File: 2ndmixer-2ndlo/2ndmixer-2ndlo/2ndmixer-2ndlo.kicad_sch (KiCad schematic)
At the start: 55 parts, among them J201 Coax Solder Point, J202 Conn_01x02, J203 Coax Solder Point, Q201 2N5179, Q202 2N5109, T201 Bifilar_Transformer, U201 MAV-11BSM+, U202 TUF-1H+, Y201 100MHz

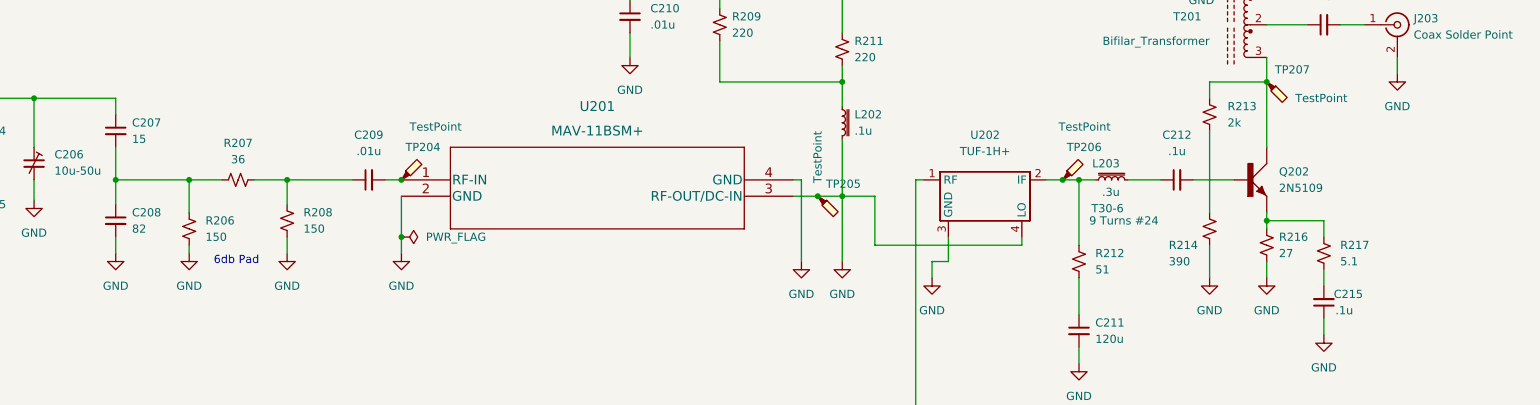
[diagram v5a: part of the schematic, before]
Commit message: added some test points
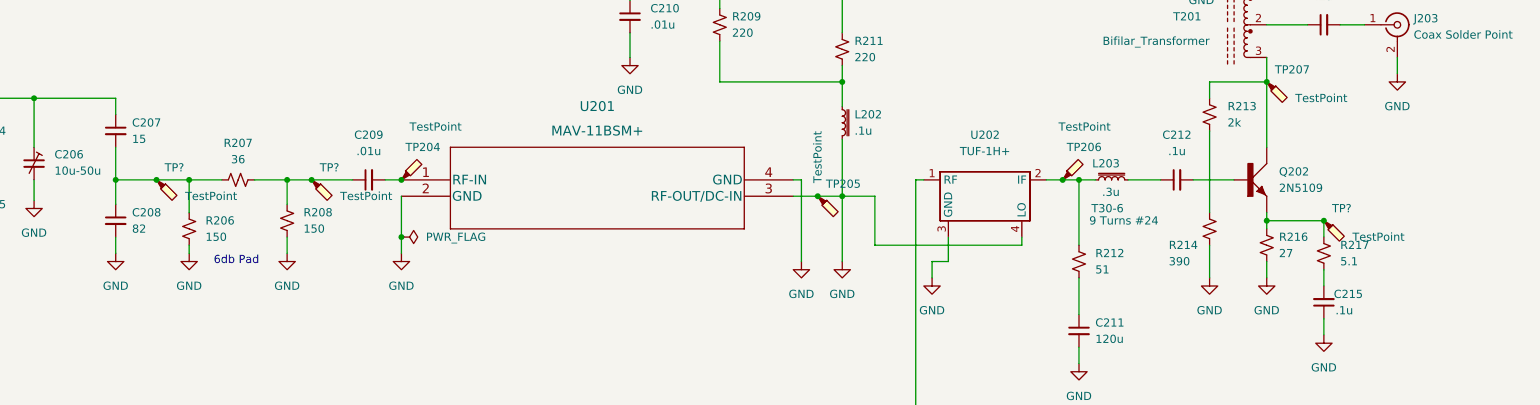
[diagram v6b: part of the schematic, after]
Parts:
- added TP? (x3): TestPoint, TestPoint:TestPoint_Pad_1.0x1.0mm, symbol Connector:TestPoint_Probe
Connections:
- net at C209.1, R207.2, R208.1: now also TP?.1
- net at Q202.E, R216.1, R217.1: now also TP?.1
- net at C207.2, C208.1, R206.1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: now also TP?.1
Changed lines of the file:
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@@
   (junction (at 49.53 69.85) (diameter 0) (color 0 0 0 0)
   )
+  (junction (at 123.19 120.65) (diameter 0) (color 0 0 0 0)
+  )
   (junction (at 295.91 105.41) (diameter 0) (color 0 0 0 0)
   )
@@
   (junction (at 43.18 97.79) (diameter 0) (color 0 0 0 0)
   )
+  (junction (at 147.32 120.65) (diameter 0) (color 0 0 0 0)
+  )
+  (junction (at 304.8 127) (diameter 0) (color 0 0 0 0)
+  )
   (junction (at 128.27 120.65) (diameter 0) (color 0 0 0 0)
   )
@@
     (stroke (width 0) (type default) (color 0 0 0 0))
   )
-  (wire (pts (xy 128.27 120.65) (xy 116.84 120.65))
+  (wire (pts (xy 128.27 120.65) (xy 123.19 120.65))
     (stroke (width 0) (type default) (color 0 0 0 0))
   )
@@
     (stroke (width 0) (type default) (color 0 0 0 0))
   )
-  (wire (pts (xy 153.67 120.65) (xy 143.51 120.65))
+  (wire (pts (xy 153.67 120.65) (xy 147.32 120.65))
     (stroke (width 0) (type default) (color 0 0 0 0))
   )
@@
     (stroke (width 0) (type default) (color 0 0 0 0))
   )
+  (wire (pts (xy 147.32 120.65) (xy 143.51 120.65))
+    (stroke (width 0) (type default) (color 0 0 0 0))
+  )
   (wire (pts (xy 311.15 96.52) (xy 307.34 96.52))
     (stroke (width 0) (type default) (color 0 0 0 0))
@@
   )
   (wire (pts (xy 229.87 82.55) (xy 229.87 69.85))
+    (stroke (width 0) (type default) (color 0 0 0 0))
+  )
+  (wire (pts (xy 123.19 120.65) (xy 116.84 120.65))
     (stroke (width 0) (type default) (color 0 0 0 0))
   )
@@
     (pin "2")
   )
+  (symbol (lib_id "Connector:TestPoint_Probe") (at 123.19 120.65 0) (mirror x) (unit 1)
+    (in_bom yes) (on_board yes)
+    (property "Reference" "TP?" (id 0) (at 124.46 118.745 0)
+      (effects (font (size 1.27 1.27)) (justify left))
+    )
+    (property "Value" "TestPoint" (id 1) (at 127.635 123.19 0)
+      (effects (font (size 1.27 1.27)) (justify left))
+    )
+    (property "Footprint" "TestPoint:TestPoint_Pad_1.0x1.0mm" (id 2) (at 128.27 120.65 0)
+      (effects (font (size 1.27 1.27)) hide)
+    )
+    (property "Datasheet" "~" (id 3) (at 128.27 120.65 0)
+      (effects (font (size 1.27 1.27)) hide)
+    )
+    (property "Spice_Netlist_Enabled" "N" (id 4) (at 123.19 120.65 0)
+      (effects (font (size 1.27 1.27)) hide)
+    )
+    (pin "1")
+  )
+  (symbol (lib_id "Connector:TestPoint_Probe") (at 147.32 120.65 0) (mirror x) (unit 1)
+    (in_bom yes) (on_board yes)
+    (property "Reference" "TP?" (id 0) (at 148.59 118.745 0)
+      (effects (font (size 1.27 1.27)) (justify left))
+    )
+    (property "Value" "TestPoint" (id 1) (at 151.765 123.19 0)
+      (effects (font (size 1.27 1.27)) (justify left))
+    )
+    (property "Footprint" "TestPoint:TestPoint_Pad_1.0x1.0mm" (id 2) (at 152.4 120.65 0)
+      (effects (font (size 1.27 1.27)) hide)
+    )
+    (property "Datasheet" "~" (id 3) (at 152.4 120.65 0)
+      (effects (font (size 1.27 1.27)) hide)
+    )
+    (property "Spice_Netlist_Enabled" "N" (id 4) (at 147.32 120.65 0)
+      (effects (font (size 1.27 1.27)) hide)
+    )
+    (pin "1")
+  )
   (symbol (lib_id "Mechanical:MountingHole") (at 178.435 189.23 0) (unit 1)
     (in_bom yes) (on_board yes) (fields_autoplaced)
@@
     (pin "2")
   )
+  (symbol (lib_id "Connector:TestPoint_Probe") (at 304.8 127 0) (mirror x) (unit 1)
+    (in_bom yes) (on_board yes)
+    (property "Reference" "TP?" (id 0) (at 306.07 125.095 0)
+      (effects (font (size 1.27 1.27)) (justify left))
+    )
+    (property "Value" "TestPoint" (id 1) (at 309.245 129.54 0)
+      (effects (font (size 1.27 1.27)) (justify left))
+    )
+    (property "Footprint" "TestPoint:TestPoint_Pad_1.0x1.0mm" (id 2) (at 309.88 127 0)
+      (effects (font (size 1.27 1.27)) hide)
+    )
+    (property "Datasheet" "~" (id 3) (at 309.88 127 0)
+      (effects (font (size 1.27 1.27)) hide)
+    )
+    (property "Spice_Netlist_Enabled" "N" (id 4) (at 304.8 127 0)
+      (effects (font (size 1.27 1.27)) hide)
+    )
+    (pin "1")
+  )
   (symbol (lib_id "Device:C_Feedthrough") (at 31.75 72.39 0) (unit 1)
     (in_bom yes) (on_board no) (fields_autoplaced)
@@
       (reference "TP207") (unit 1) (value "TestPoint") (footprint "TestPoint:TestPoint_Pad_1.0x1.0mm")
     )
+    (path "/3076ed7b-0b06-4ea4-ba72-ad5a1845b382"
+      (reference "TP?") (unit 1) (value "TestPoint") (footprint "TestPoint:TestPoint_Pad_1.0x1.0mm")
+    )
+    (path "/38003388-8080-4693-82ad-14b5f8202bb9"
+      (reference "TP?") (unit 1) (value "TestPoint") (footprint "TestPoint:TestPoint_Pad_1.0x1.0mm")
+    )
+    (path "/d3bb7f25-1006-43ac-a22f-03cbe6a0bb45"
+      (reference "TP?") (unit 1) (value "TestPoint") (footprint "TestPoint:TestPoint_Pad_1.0x1.0mm")
+    )
     (path "/ebf3feb7-ceae-4077-b06e-4689b0114722"

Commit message: updates to 2ndmixer-2ndlo
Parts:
- removed C214: .1u, Capacitor_THT:C_Disc_D5.0mm_W2.5mm_P5.00mm, symbol Device:C_Small
- removed Q202: 2N5109, TO5A, symbol 2N5109:2N5109
- added L202: 420n, Inductor_THT:L_Toroid_Vertical_L13.0mm_W6.5mm_P5.60mm, symbol Device:L_Iron_Small
- added Q202: 2N5179, 2ndmixer-2ndlo:TO127P584H533-4N, symbol 2ndmixer-2ndlo:2N5179
- C204: value 15 -> 33
- C205: value 82 -> 33
- C211: value 120u -> 120p
- L201: value 57n -> 40n; Field4 5 turns #22 -> 4 turns #22
- L203: renamed from L202; value .1u -> 1u; Field4 (none) -> T30-6; Field5 (none) -> 10T #30
- L204: renamed from L203; value .3u -> 1u; Field5 9 Turns #24 -> 10T #30
- gave numbers to parts that had none: 3
- renumbered C203 to C201, C201 to C202, C202 to C203, C215 to C214, R203 to R202, R202 to R203, TP204 to TP206, TP205 to TP207, TP206 to TP208, TP207 to TP209
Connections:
- net GND: now also Q202.4 (SHIELD)
- net at T201.2: now also J203.1 (In)
- net at R216.1, R217.1, TP210.1: now also Q202.1
- net at Q201.1, R205.1, TP203.1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: now also L202.2
- net at C204.2, C205.1, Y201.2: now also L202.1
- net at C212.2: now also Q202.2
- net at R213.1, T201.3, TP209.1: now also Q202.3
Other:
- note added: "Notes: -Digikey does not have 82u caps -Seems like 100Mhz 5th overtone xtal is special order -MAV-11 is available but not on Digi-Key and as a surface mount -TUF-1H+ not on Digi-Key but avaialble from MiniCircuits"
- note removed: "Notes: -Digikey does not have 82u caps -Seems like 100Mhz 5th overtone xtal is special order -MAV-11 is available but not on Digi-Key and as a surface mount -TUF-1H+ not on Digi-Key but avaialble from MiniCircuits -2N5109 is obsolete"
- moved on the sheet: C201, C205, C214, R202, R203, R205, R211, R216, R217, TP210
